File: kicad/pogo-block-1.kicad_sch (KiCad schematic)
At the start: 23 parts, among them J3 ALT_BP_L, J4 ALT_BP_R, SW1 GAIN_MAIN, SW2 GAIN_BP3, U2 OPA1612, U3 OPA1612

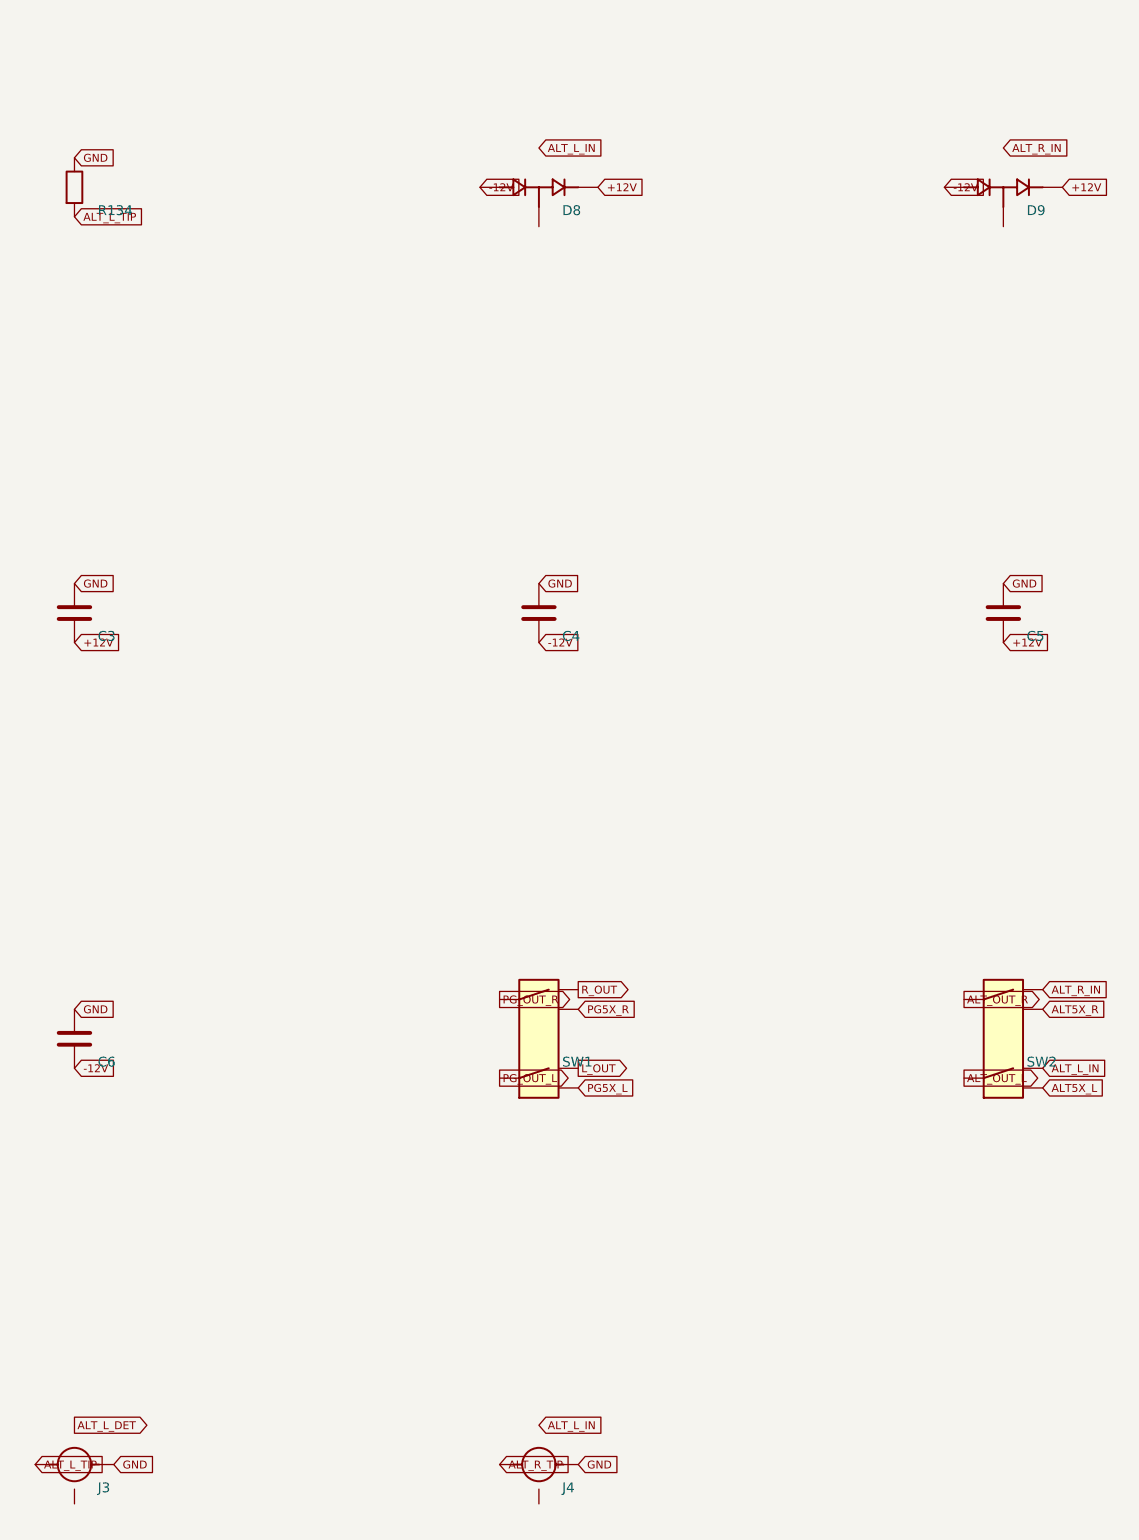
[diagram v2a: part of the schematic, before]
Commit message: 0020 §E: make ALT_BP_L/R fully independent (Lane A plugin + hardware)
User direction: instead of a dual-switch jack (which would break the M8 panel
standard) to reproduce the R->L normal, make ALT L and R INDEPENDENT. This
dissolves the §E problem - each jack self-detects via its own switch lug, no
new part, no panel change, cleaner stereo behavior.

PLUGIN (Lane A; G3 pending in VCV Rack):
- Pogo.cpp: altR = altRConn ? PreGain(...) : 0 (dropped R->L normal);
  bp3InR = altRConn ? VcaBlock(...) : bandR (was altLConn||altRConn). L same.
- plugin.json 2.0.0 -> 2.1.0.

HARDWARE (follows):
- block-1: J4 mirrors J3 -> ALT_R_DET:[J4.3] + R225 22k tip pulldown; removed
  J4.3 from ALT_L_IN (R->L normal gone). New boundary ALT_R_DET.
- block-6-dist3: split U81 selects - X/L (pin11) stays ALT_L_DET; Y/R (pin10)
  now ALT_R_DET + R226 100k pull-up. New boundary ALT_R_DET.
- components.yaml +R225 +R226 (no new part type). Regenerated sch/BOM/viz.

All --check gates green; ALT_R_DET boundary resolves across both sheets.
Reclassifies 0020 as A/B mixed. Supersedes the dual-switch-jack plan.

https://claude.ai/code/session_013jFXG5oeMVSYP7iRpwGvtQ
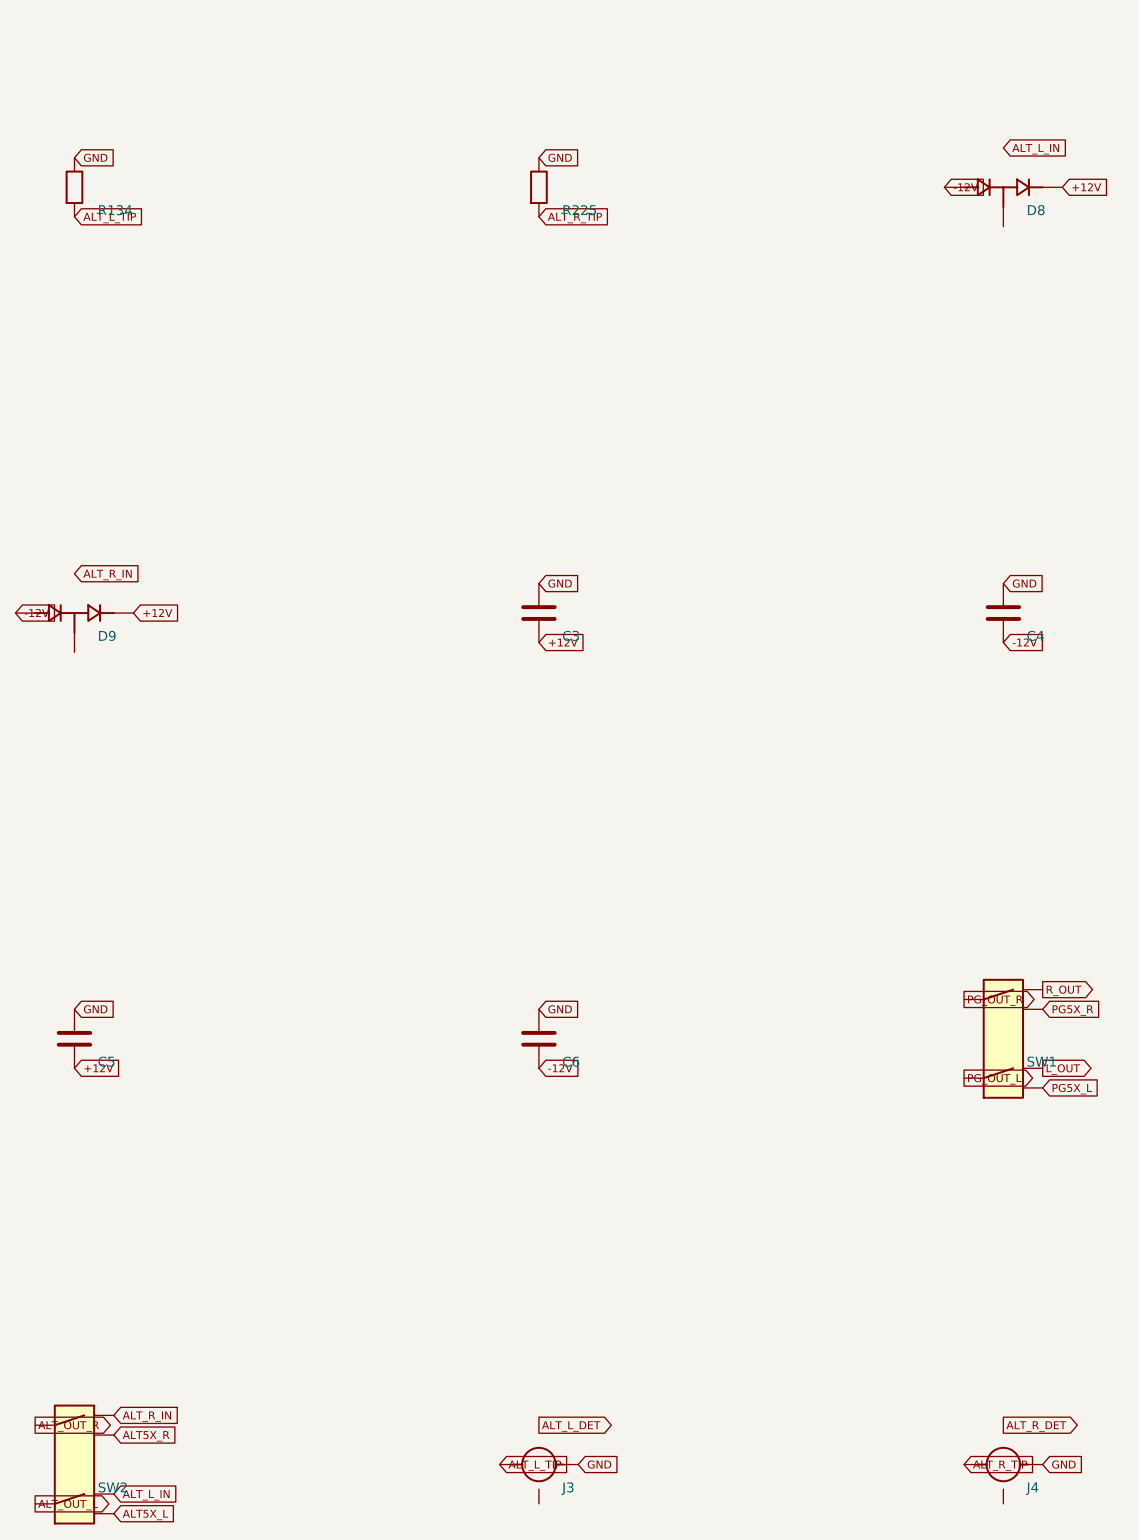
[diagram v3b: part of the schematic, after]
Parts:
- added J4: ALT_BP_R, POGO_Connector_Audio:Jack_3.5mm_QingPu_WQP-PJ398SM_Vertical_CircularHoles, symbol Device:Audio_Jack_3.5mm_SwitchT
- C6: renamed from SW1; value GAIN_MAIN -> 100nF; footprint POGO_Button_Switch_THT:SW_Dailywell_DW3_DPDT -> (none); symbol Switch:SW_Dailywell_DW3 -> Device:C
- D9: renamed from C3; value 100nF -> BAT54S; footprint (none) -> POGO_Package_TO_SOT_SMD:SOT-23; symbol Device:C -> Diode:BAT54S
- J3: renamed from J4; value ALT_BP_R -> ALT_BP_L
- R225: renamed from D8; value BAT54S -> 22k; footprint POGO_Package_TO_SOT_SMD:SOT-23 -> (none); symbol Diode:BAT54S -> Device:R
- SW1: renamed from SW2; value GAIN_BP3 -> GAIN_MAIN
- SW2: renamed from J3; value ALT_BP_L -> GAIN_BP3; footprint POGO_Connector_Audio:Jack_3.5mm_QingPu_WQP-PJ398SM_Vertical_CircularHoles -> POGO_Button_Switch_THT:SW_Dailywell_DW3_DPDT; symbol Device:Audio_Jack_3.5mm_SwitchT -> Switch:SW_Dailywell_DW3
- renumbered C4 to C3, C5 to C4, C6 to C5, D9 to D8
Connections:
- net +12V: now also C3.2, C5.2; no longer C4.2, R225.2 (K2)
- net -12V: now also C4.2, C6.2, D9.1 (A1); no longer C3.2, C5.2, R225.1 (A1)
- net ALT5X_L: now also SW2.6 (B2); no longer SW1.6 (B2)
- net ALT5X_R: now also SW2.3 (A2); no longer SW1.3 (A2)
- net ALT_L_IN: now also SW2.4 (B1); no longer SW1.4 (B1)
- net ALT_L_TIP: now also J3.1 (T); no longer SW2.1 (T)
- net ALT_OUT_L: now also SW2.5 (B_COM); no longer SW1.5 (B_COM)
- net ALT_OUT_R: now also SW2.2 (A_COM); no longer SW1.2 (A_COM)
- net ALT_R_IN: now also SW2.1 (A1); no longer SW1.1 (A1)
- net ALT_R_TIP: now also R225.2, J4.1 (T); no longer J3.1 (T)
- net GND: now also C6.1, R225.1, J4.2 (S); no longer D9.1, SW2.2 (S)
- net L_OUT: now also SW1.4 (B1); no longer C6.4 (B1)
- net PG5X_L: now also SW1.6 (B2); no longer C6.6 (B2)
- net PG5X_R: now also SW1.3 (A2); no longer C6.3 (A2)
- net PG_OUT_L: now also SW1.5 (B_COM); no longer C6.5 (B_COM)
- net PG_OUT_R: now also SW1.2 (A_COM); no longer C6.2 (A_COM)
- net R_OUT: now also SW1.1 (A1); no longer C6.1 (A1)
